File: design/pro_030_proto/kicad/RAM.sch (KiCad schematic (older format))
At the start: 8 parts, among them U1 AS6C4008-55TIN, U2 AS6C4008-55TIN, U3 AS6C4008-55TIN, U4 AS6C4008-55TIN

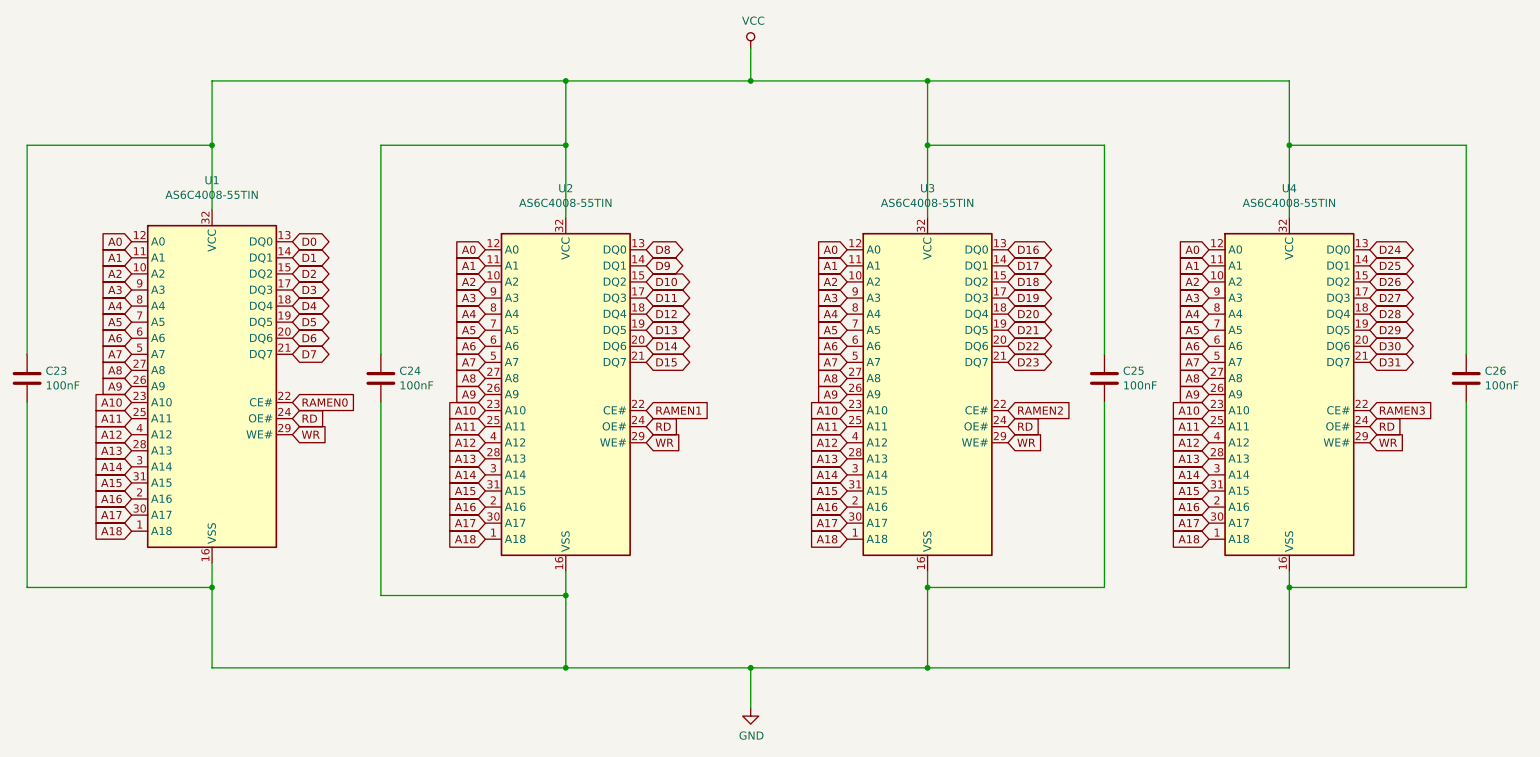
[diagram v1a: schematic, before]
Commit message: Largeish changeset:
* Added (first-cut) glue for DTACK generation
* Fix mem selects to use new DTACK generation
* Add missing footprints for Kicad
* Add POWER and TESTPOINTS schematics
* Update footprints across the board to allow error-free PCB import
* Pull all components (so far) into PCB
* Fix MC68030RC footprint (missing pads)
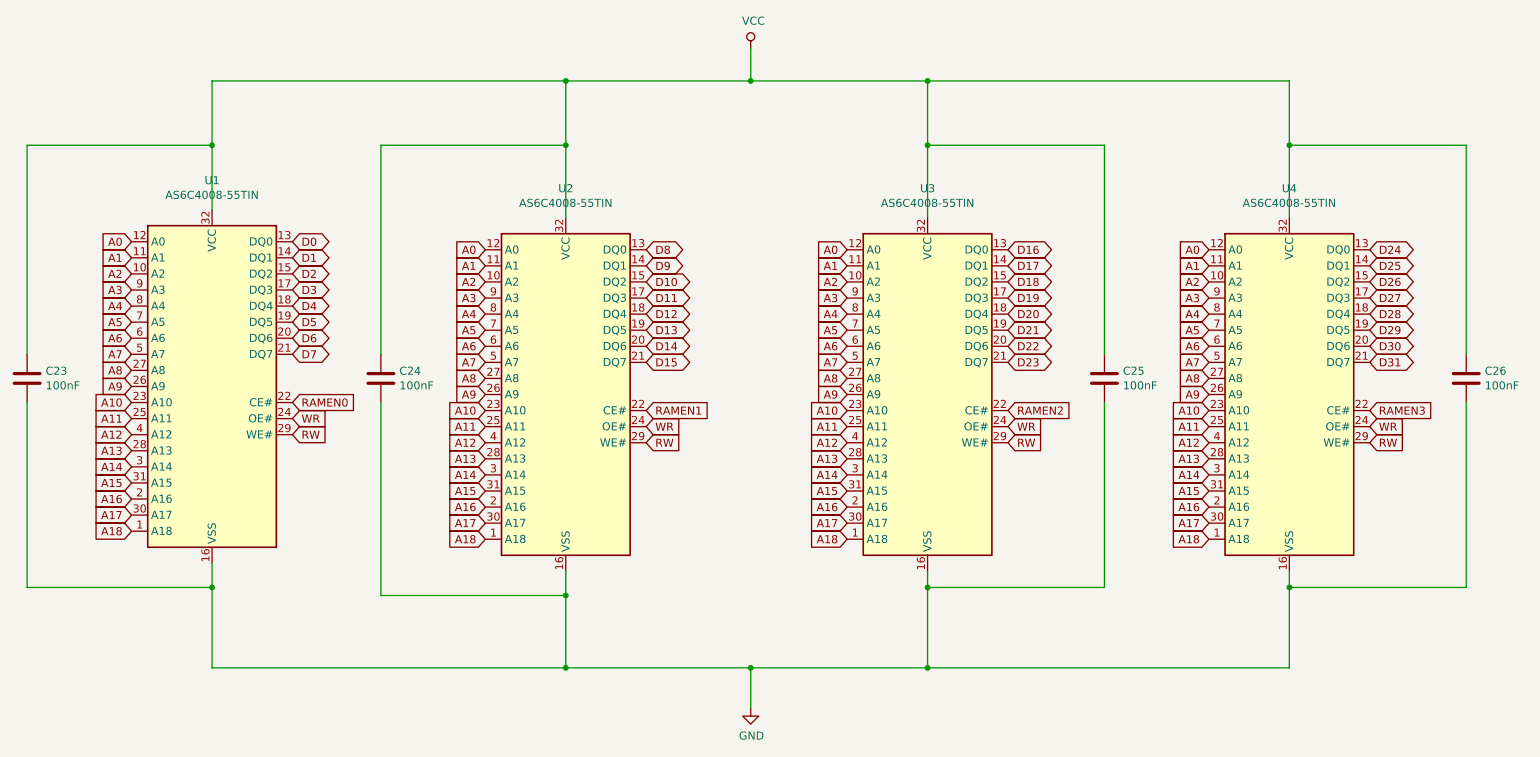
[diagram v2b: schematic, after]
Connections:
- net RD is gone; now on net WR: U1.24 (OE#), U2.24 (OE#), U3.24 (OE#), U4.24 (OE#)
- net WR: no longer U1.29 (WE#), U2.29 (WE#), U3.29 (WE#), U4.29 (WE#)
- new net RW: U1.29 (WE#), U2.29 (WE#), U3.29 (WE#), U4.29 (WE#)
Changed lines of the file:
@@
 $Descr A4 11693 8268
 encoding utf-8
-Sheet 3 8
+Sheet 3 10
 Title "rosco_m68k Pro (030) Prototype"
-Date "2021-07-16"
+Date "2021-07-24"
 Rev "0"
 Comp "The Really Old-School Company Limited"
@@
 	4500 5150 4500 5600
 Text GLabel 2800 4150 2    50   Input ~ 0
+RW
+Text GLabel 2800 4050 2    50   Input ~ 0
 WR
-Text GLabel 2800 4050 2    50   Input ~ 0
-RD
 Text GLabel 2800 3950 2    50   Input ~ 0
 RAMEN0
 Text GLabel 5000 4200 2    50   Input ~ 0
+RW
+Text GLabel 5000 4100 2    50   Input ~ 0
 WR
-Text GLabel 5000 4100 2    50   Input ~ 0
-RD
 Text GLabel 5000 4000 2    50   Input ~ 0
 RAMEN1
 Text GLabel 7250 4200 2    50   Input ~ 0
+RW
+Text GLabel 7250 4100 2    50   Input ~ 0
 WR
-Text GLabel 7250 4100 2    50   Input ~ 0
-RD
 Text GLabel 7250 4000 2    50   Input ~ 0
 RAMEN2
 Text GLabel 9500 4200 2    50   Input ~ 0
+RW
+Text GLabel 9500 4100 2    50   Input ~ 0
 WR
-Text GLabel 9500 4100 2    50   Input ~ 0
-RD
 Text GLabel 9500 4000 2    50   Input ~ 0
 RAMEN3

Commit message: Interrupts + Xosera schematic, re-annotate
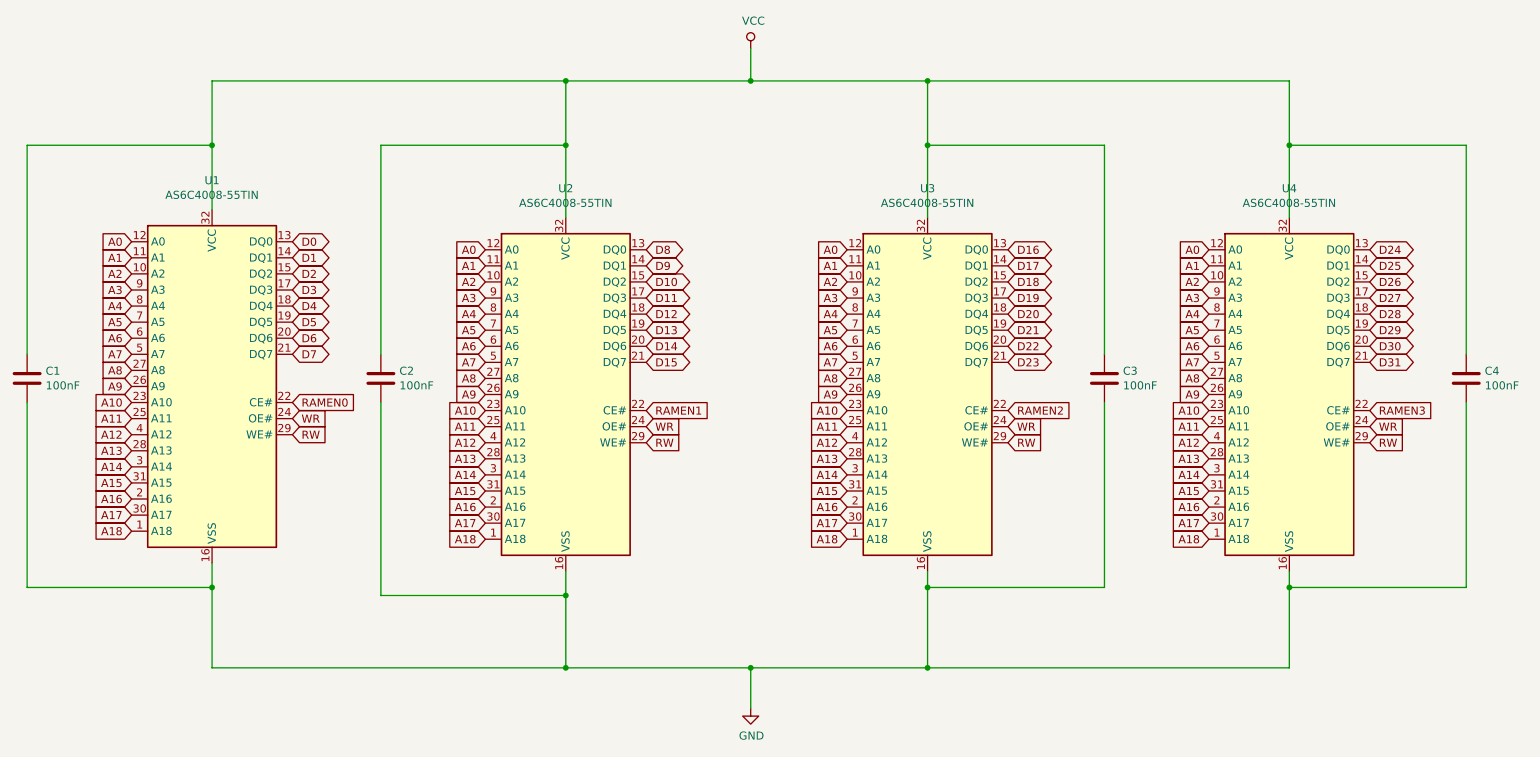
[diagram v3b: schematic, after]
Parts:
- renumbered C23 to C1, C24 to C2, C25 to C3, C26 to C4
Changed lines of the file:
@@
 $Descr A4 11693 8268
 encoding utf-8
-Sheet 3 10
+Sheet 3 13
 Title "rosco_m68k Pro (030) Prototype"
 Date "2021-07-24"
@@
 D31
 $Comp
-L power:VCC #PWR07
+L power:VCC #PWR08
 U 1 1 60F4C3C9
 P 5650 1750
-F 0 "#PWR07" H 5650 1600 50  0001 C CNN
+F 0 "#PWR08" H 5650 1600 50  0001 C CNN
 F 1 "VCC" H 5667 1923 50  0000 C CNN
 F 2 "" H 5650 1750 50  0001 C CNN
@@
 	5650 1950 6750 1950
 $Comp
-L power:GND #PWR08
+L power:GND #PWR09
 U 1 1 60F4DB93
 P 5650 5850
-F 0 "#PWR08" H 5650 5600 50  0001 C CNN
+F 0 "#PWR09" H 5650 5600 50  0001 C CNN
 F 1 "GND" H 5655 5677 50  0000 C CNN
 F 2 "" H 5650 5850 50  0001 C CNN
@@
 Connection ~ 6750 5600
 $Comp
-L Device:C C23
+L Device:C C1
 U 1 1 60F4FBAB
 P 1150 3800
-F 0 "C23" H 1265 3846 50  0000 L CNN
+F 0 "C1" H 1265 3846 50  0000 L CNN
 F 1 "100nF" H 1265 3755 50  0000 L CNN
 F 2 "Capacitor_THT:C_Rect_L4.0mm_W2.5mm_P2.50mm" H 1188 3650 50  0001 C CNN
@@
 	2300 5100 2300 5600
 $Comp
-L Device:C C24
+L Device:C C2
 U 1 1 60F51E84
 P 3350 3800
-F 0 "C24" H 3465 3846 50  0000 L CNN
+F 0 "C2" H 3465 3846 50  0000 L CNN
 F 1 "100nF" H 3465 3755 50  0000 L CNN
 F 2 "Capacitor_THT:C_Rect_L4.0mm_W2.5mm_P2.50mm" H 3388 3650 50  0001 C CNN
@@
 $EndComp
 $Comp
-L Device:C C25
+L Device:C C3
 U 1 1 60F5278F
 P 7850 3800
-F 0 "C25" H 7965 3846 50  0000 L CNN
+F 0 "C3" H 7965 3846 50  0000 L CNN
 F 1 "100nF" H 7965 3755 50  0000 L CNN
 F 2 "Capacitor_THT:C_Rect_L4.0mm_W2.5mm_P2.50mm" H 7888 3650 50  0001 C CNN
@@
 $EndComp
 $Comp
-L Device:C C26
+L Device:C C4
 U 1 1 60F5320A
 P 10100 3800
-F 0 "C26" H 10215 3846 50  0000 L CNN
+F 0 "C4" H 10215 3846 50  0000 L CNN
 F 1 "100nF" H 10215 3755 50  0000 L CNN
 F 2 "Capacitor_THT:C_Rect_L4.0mm_W2.5mm_P2.50mm" H 10138 3650 50  0001 C CNN

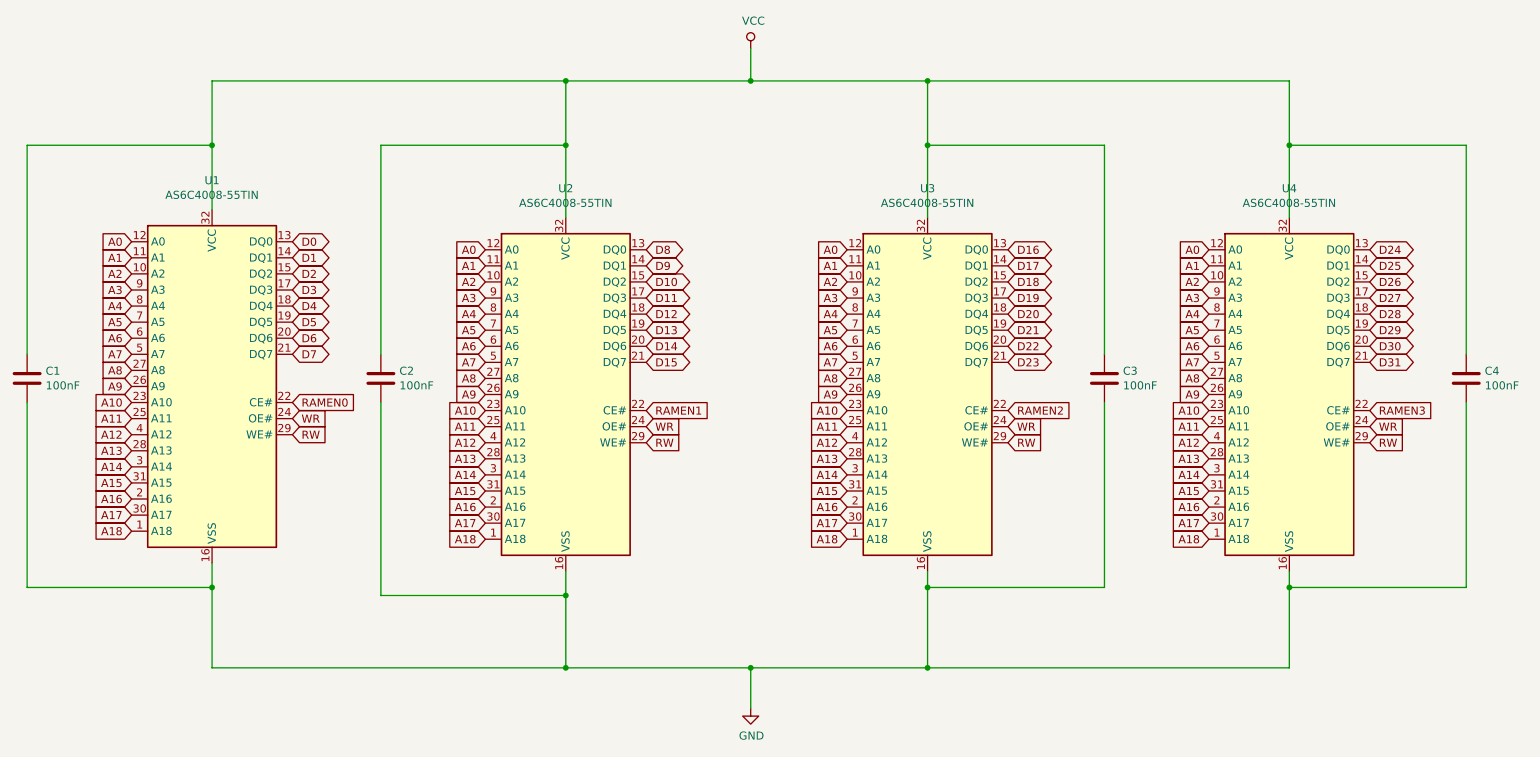
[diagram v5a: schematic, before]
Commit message: Lots more changes
* Add DIN expansion connectors (provisional pinout)
* Fix incorrect address lines for RAM & ROM (Doh!)
* Remove unused level shifters
* Fix clock enables
* Lots of other small fixes
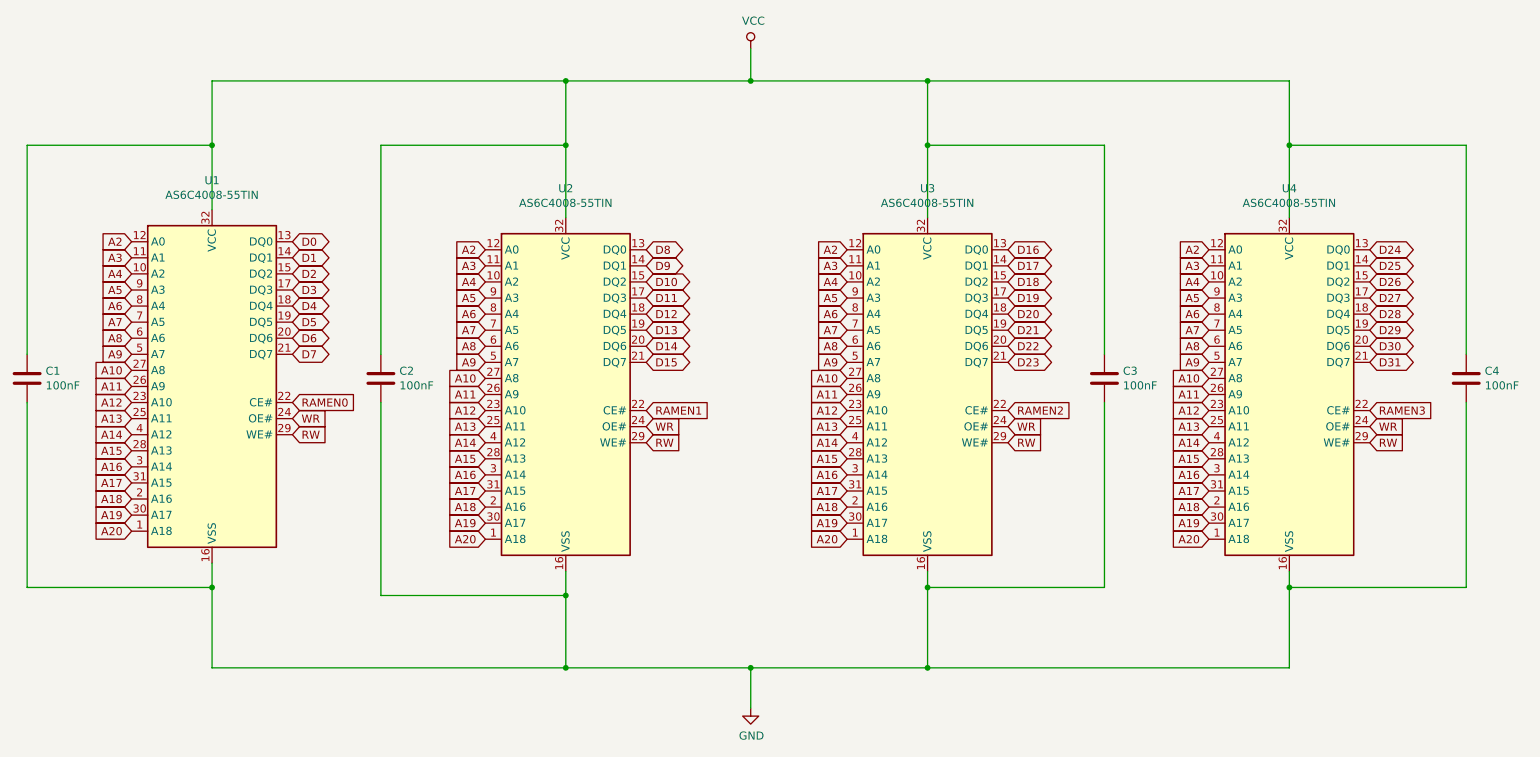
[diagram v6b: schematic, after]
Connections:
- net A0 is gone; now on net A2: U1.12 (A0), U2.12 (A0), U3.12 (A0), U4.12 (A0)
- net A1 is gone; now on net A3: U1.11 (A1), U2.11 (A1), U3.11 (A1), U4.11 (A1)
- net A10: now also U1.27 (A8), U2.27 (A8), U3.27 (A8), U4.27 (A8); no longer U1.23 (A10), U2.23 (A10), U3.23 (A10), U4.23 (A10)
- net A11: now also U1.26 (A9), U2.26 (A9), U3.26 (A9), U4.26 (A9); no longer U1.25 (A11), U2.25 (A11), U3.25 (A11), U4.25 (A11)
- net A12: now also U1.23 (A10), U2.23 (A10), U3.23 (A10), U4.23 (A10); no longer U1.4 (A12), U2.4 (A12), U3.4 (A12), U4.4 (A12)
- net A13: now also U1.25 (A11), U2.25 (A11), U3.25 (A11), U4.25 (A11); no longer U1.28 (A13), U2.28 (A13), U3.28 (A13), U4.28 (A13)
- net A14: now also U1.4 (A12), U2.4 (A12), U3.4 (A12), U4.4 (A12); no longer U1.3 (A14), U2.3 (A14), U3.3 (A14), U4.3 (A14)
- net A15: now also U1.28 (A13), U2.28 (A13), U3.28 (A13), U4.28 (A13); no longer U1.31 (A15), U2.31 (A15), U3.31 (A15), U4.31 (A15)
- net A16: now also U1.3 (A14), U2.3 (A14), U3.3 (A14), U4.3 (A14); no longer U1.2 (A16), U2.2 (A16), U3.2 (A16), U4.2 (A16)
- net A17: now also U1.31 (A15), U2.31 (A15), U3.31 (A15), U4.31 (A15); no longer U1.30 (A17), U2.30 (A17), U3.30 (A17), U4.30 (A17)
- net A18: now also U1.2 (A16), U2.2 (A16), U3.2 (A16), U4.2 (A16); no longer U1.1 (A18), U2.1 (A18), U3.1 (A18), U4.1 (A18)
- net A2: no longer U1.10 (A2), U2.10 (A2), U3.10 (A2), U4.10 (A2)
- net A3: no longer U1.9 (A3), U2.9 (A3), U3.9 (A3), U4.9 (A3)
- net A4: now also U1.10 (A2), U2.10 (A2), U3.10 (A2), U4.10 (A2); no longer U1.8 (A4), U2.8 (A4), U3.8 (A4), U4.8 (A4)
- net A5: now also U1.9 (A3), U2.9 (A3), U3.9 (A3), U4.9 (A3); no longer U1.7 (A5), U2.7 (A5), U3.7 (A5), U4.7 (A5)
- net A6: now also U1.8 (A4), U2.8 (A4), U3.8 (A4), U4.8 (A4); no longer U1.6 (A6), U2.6 (A6), U3.6 (A6), U4.6 (A6)
- net A7: now also U1.7 (A5), U2.7 (A5), U3.7 (A5), U4.7 (A5); no longer U1.5 (A7), U2.5 (A7), U3.5 (A7), U4.5 (A7)
- net A8: now also U1.6 (A6), U2.6 (A6), U3.6 (A6), U4.6 (A6); no longer U1.27 (A8), U2.27 (A8), U3.27 (A8), U4.27 (A8)
- net A9: now also U1.5 (A7), U2.5 (A7), U3.5 (A7), U4.5 (A7); no longer U1.26 (A9), U2.26 (A9), U3.26 (A9), U4.26 (A9)
- new net A19: U1.30 (A17), U2.30 (A17), U3.30 (A17), U4.30 (A17)
- new net A20: U1.1 (A18), U2.1 (A18), U3.1 (A18), U4.1 (A18)
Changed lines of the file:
@@
 $Descr A4 11693 8268
 encoding utf-8
-Sheet 3 15
+Sheet 3 14
 Title "rosco_m68k Pro (030) Prototype"
 Date "2021-10-01"
@@
 $EndComp
 Text GLabel 1800 2950 0    50   Input ~ 0
-A0
+A2
 Text GLabel 1800 3050 0    50   Input ~ 0
-A1
+A3
 Text GLabel 1800 3150 0    50   Input ~ 0
-A2
+A4
 Text GLabel 1800 3250 0    50   Input ~ 0
-A3
+A5
 Text GLabel 1800 3350 0    50   Input ~ 0
-A4
+A6
 Text GLabel 1800 3450 0    50   Input ~ 0
-A5
+A7
 Text GLabel 1800 3550 0    50   Input ~ 0
-A6
+A8
 Text GLabel 1800 3650 0    50   Input ~ 0
-A7
+A9
 Text GLabel 1800 3750 0    50   Input ~ 0
-A8
+A10
 Text GLabel 1800 3850 0    50   Input ~ 0
-A9
+A11
 Text GLabel 1800 3950 0    50   Input ~ 0
-A10
+A12
 Text GLabel 1800 4050 0    50   Input ~ 0
-A11
+A13
 Text GLabel 1800 4150 0    50   Input ~ 0
-A12
+A14
 Text GLabel 1800 4250 0    50   Input ~ 0
-A13
+A15
 Text GLabel 1800 4350 0    50   Input ~ 0
-A14
+A16
 Text GLabel 1800 4450 0    50   Input ~ 0
-A15
+A17
 Text GLabel 1800 4550 0    50   Input ~ 0
-A16
-Text GLabel 1800 4650 0    50   Input ~ 0
-A17
-Text GLabel 1800 4750 0    50   Input ~ 0
 A18
 Text GLabel 4000 3000 0    50   Input ~ 0
-A0
+A2
 Text GLabel 4000 3100 0    50   Input ~ 0
-A1
+A3
 Text GLabel 4000 3200 0    50   Input ~ 0
-A2
+A4
 Text GLabel 4000 3300 0    50   Input ~ 0
-A3
+A5
 Text GLabel 4000 3400 0    50   Input ~ 0
-A4
+A6
 Text GLabel 4000 3500 0    50   Input ~ 0
-A5
+A7
 Text GLabel 4000 3600 0    50   Input ~ 0
-A6
+A8
 Text GLabel 4000 3700 0    50   Input ~ 0
-A7
+A9
 Text GLabel 4000 3800 0    50   Input ~ 0
-A8
+A10
 Text GLabel 4000 3900 0    50   Input ~ 0
-A9
+A11
 Text GLabel 4000 4000 0    50   Input ~ 0
-A10
+A12
 Text GLabel 4000 4100 0    50   Input ~ 0
-A11
+A13
 Text GLabel 4000 4200 0    50   Input ~ 0
-A12
+A14
 Text GLabel 4000 4300 0    50   Input ~ 0
-A13
+A15
 Text GLabel 4000 4400 0    50   Input ~ 0
-A14
+A16
 Text GLabel 4000 4500 0    50   Input ~ 0
-A15
+A17
 Text GLabel 4000 4600 0    50   Input ~ 0
-A16
-Text GLabel 4000 4700 0    50   Input ~ 0
-A17
-Text GLabel 4000 4800 0    50   Input ~ 0
 A18
 Text GLabel 6250 3000 0    50   Input ~ 0
-A0
+A2
 Text GLabel 6250 3100 0    50   Input ~ 0
-A1
+A3
 Text GLabel 6250 3200 0    50   Input ~ 0
-A2
+A4
 Text GLabel 6250 3300 0    50   Input ~ 0
-A3
+A5
 Text GLabel 6250 3400 0    50   Input ~ 0
-A4
+A6
 Text GLabel 6250 3500 0    50   Input ~ 0
-A5
+A7
 Text GLabel 6250 3600 0    50   Input ~ 0
-A6
+A8
 Text GLabel 6250 3700 0    50   Input ~ 0
-A7
+A9
 Text GLabel 6250 3800 0    50   Input ~ 0
-A8
+A10
 Text GLabel 6250 3900 0    50   Input ~ 0
-A9
+A11
 Text GLabel 6250 4000 0    50   Input ~ 0
-A10
+A12
 Text GLabel 6250 4100 0    50   Input ~ 0
-A11
+A13
 Text GLabel 6250 4200 0    50   Input ~ 0
-A12
+A14
 Text GLabel 6250 4300 0    50   Input ~ 0
-A13
+A15
 Text GLabel 6250 4400 0    50   Input ~ 0
-A14
+A16
 Text GLabel 6250 4500 0    50   Input ~ 0
-A15
+A17
 Text GLabel 6250 4600 0    50   Input ~ 0
-A16
-Text GLabel 6250 4700 0    50   Input ~ 0
-A17
-Text GLabel 6250 4800 0    50   Input ~ 0
 A18
 Text GLabel 8500 3000 0    50   Input ~ 0
-A0
+A2
 Text GLabel 8500 3100 0    50   Input ~ 0
-A1
+A3
 Text GLabel 8500 3200 0    50   Input ~ 0
-A2
+A4
 Text GLabel 8500 3300 0    50   Input ~ 0
-A3
+A5
 Text GLabel 8500 3400 0    50   Input ~ 0
-A4
+A6
 Text GLabel 8500 3500 0    50   Input ~ 0
-A5
+A7
 Text GLabel 8500 3600 0    50   Input ~ 0
-A6
+A8
 Text GLabel 8500 3700 0    50   Input ~ 0
-A7
+A9
 Text GLabel 8500 3800 0    50   Input ~ 0
-A8
+A10
 Text GLabel 8500 3900 0    50   Input ~ 0
-A9
+A11
 Text GLabel 8500 4000 0    50   Input ~ 0
-A10
+A12
 Text GLabel 8500 4100 0    50   Input ~ 0
-A11
+A13
 Text GLabel 8500 4200 0    50   Input ~ 0
-A12
+A14
 Text GLabel 8500 4300 0    50   Input ~ 0
-A13
+A15
 Text GLabel 8500 4400 0    50   Input ~ 0
-A14
+A16
 Text GLabel 8500 4500 0    50   Input ~ 0
-A15
+A17
 Text GLabel 8500 4600 0    50   Input ~ 0
-A16
-Text GLabel 8500 4700 0    50   Input ~ 0
-A17
-Text GLabel 8500 4800 0    50   Input ~ 0
 A18
 Text GLabel 2800 2950 2    50   BiDi ~ 0
@@
 Wire Wire Line
 	5650 1950 6750 1950
+Text GLabel 1800 4650 0    50   Input ~ 0
+A19
+Text GLabel 1800 4750 0    50   Input ~ 0
+A20
+Text GLabel 4000 4700 0    50   Input ~ 0
+A19
+Text GLabel 4000 4800 0    50   Input ~ 0
+A20
+Text GLabel 6250 4700 0    50   Input ~ 0
+A19
+Text GLabel 6250 4800 0    50   Input ~ 0
+A20
+Text GLabel 8500 4700 0    50   Input ~ 0
+A19
+Text GLabel 8500 4800 0    50   Input ~ 0
+A20
 $EndSCHEMATC
